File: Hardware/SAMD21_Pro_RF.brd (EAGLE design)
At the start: 40.6 x 30.5 mm, 127 parts, among them J10 AVR_SPI_PROG_3X2TESTPOINTS, J12 JST, J13 U.FL, J7 PTH, J9 External On/Off, U1 MCP73831, U2 915MHz, U4 ATSAMD21G, U5 4MB Flash, U6 3.3V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

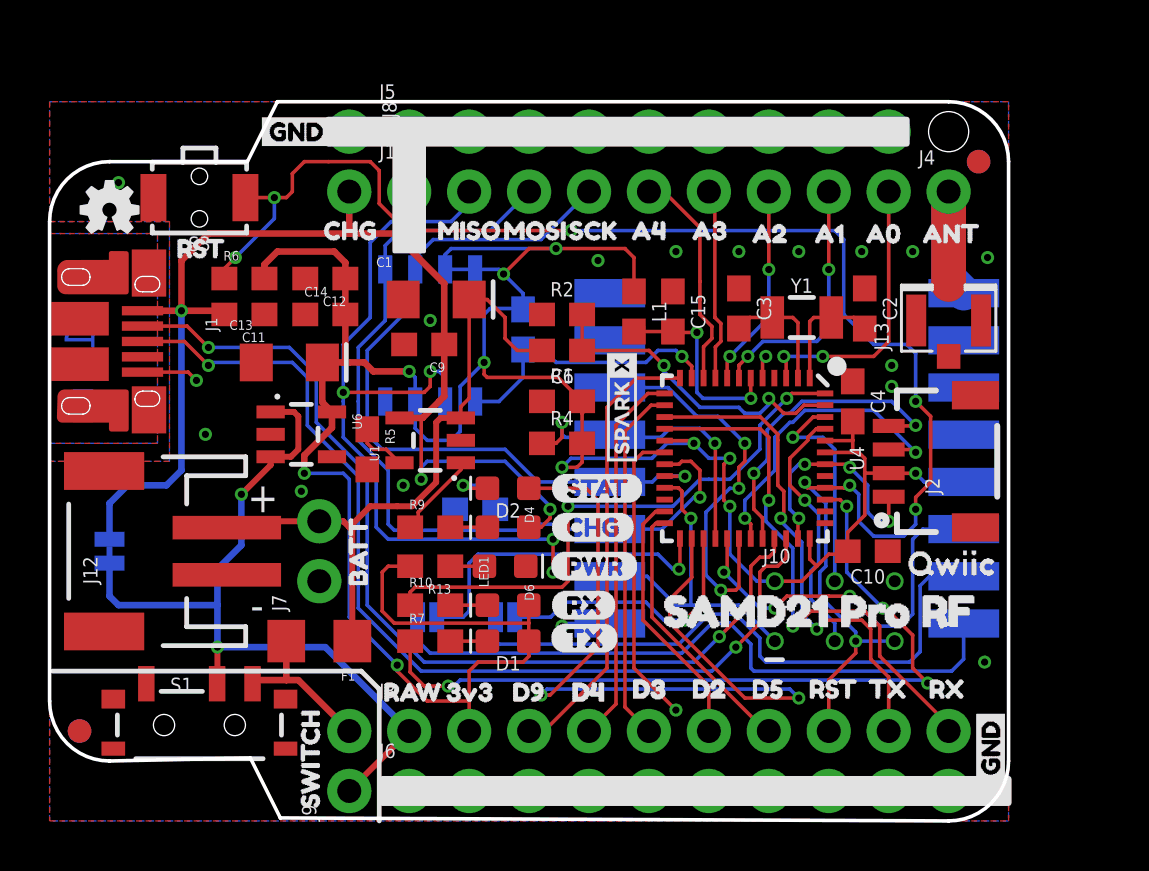
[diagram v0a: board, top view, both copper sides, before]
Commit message: Added Sparkfun labels, correct RFM module (same pinout), fixed silk
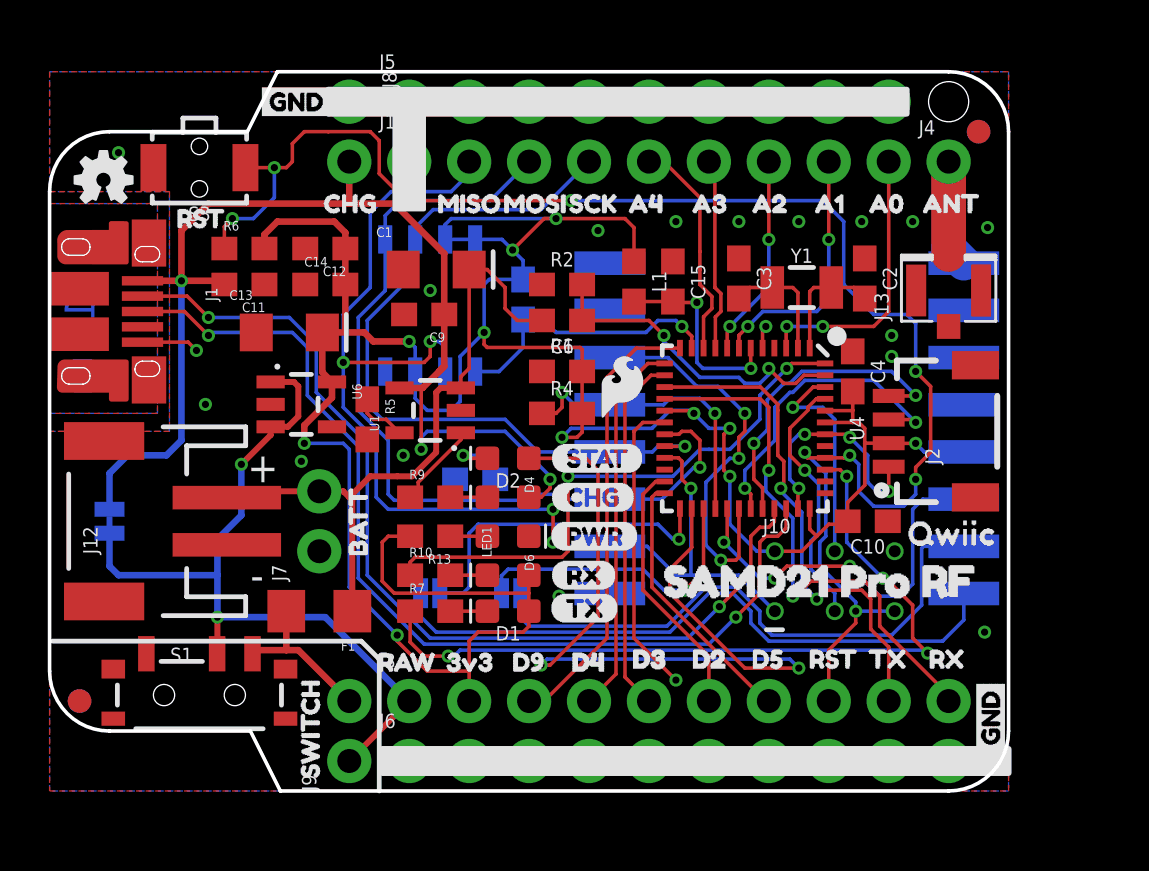
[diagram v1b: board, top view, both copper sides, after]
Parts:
- removed JP1, JP2: (no value), SparkFun-Jumpers:SMT-JUMPER_2_NO_SILK
- removed U$51: (no value), SparkX:SPARKX-MEDIUM
- removed U2: 915MHz, SparkFun-RF:RFM69HCW-XXXS2
- added JP3, JP4: (no value), SparkFun-Jumpers:SMT-JUMPER_2_NO_SILK
- added LOGO2: SFE_LOGO_NAME.1_INCH, SparkFun-Aesthetics:SFE_LOGO_NAME_.1
- added U3: RFM96W, SparkX:RFM95/96/97/98W
- U$34: value SPARKX-LOGO2 -> (none); device SparkX:SPARKX-TINY -> SparkFun-Aesthetics:SFE_LOGO_FLAME_.1
- moved U$30 1.91 mm to (8.38, 16.5)
- moved U$41 1.52 mm to (34.7, 5.59)
- moved U$57 1.52 mm to (37.0, 5.59)
- moved U$19 1.40 mm to (39.5, 5.59)
- moved U$2 1.40 mm to (29.3, 5.59)
- moved U$21 1.40 mm to (26.8, 5.59)
- moved U$33 1.40 mm to (31.8, 5.59)
- moved U$34 1.37 mm to (23.1, 15.5), turned to 0 degrees
- moved U$24 1.30 mm to (13.2, 5.46)
- moved LOGO1 1.30 mm to (2.29, 25.9)
- moved U$61 1.30 mm to (2.29, 25.9)
- moved LED1 1.28 mm to (19.4, 10.8)
- moved U$7 1.28 mm to (34.0, 24.9)
- moved C9 1.27 mm to (15.9, 20.2)
- moved J11 1.27 mm to (15.2, 26.7)
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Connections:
- removed net D10: JP1.2, U4.27
- removed net D11: JP2.2, U4.25
- removed net RFM_IO1: JP1.1, U2.15
- removed net RFM_IO2: JP2.1, U2.16
- new net D10_LORA-WAN: JP3.2, U4.27
- new net D11_LORA-WAN: JP4.2, U4.25
- new net N$17: JP3.1, U3.DIO1
- new net N$18: JP4.1, U3.DIO2
- net !RFM_CS: now also U3.NSS; no longer U2.5
- net 3.3V: now also U3.3.3V; no longer U2.13
- net ANT: now also U3.ANT; no longer U2.9
- net GND: now also U3.GND@1, U3.GND@2, U3.GND@3; no longer U2.1, U2.10, U2.8
- net MISO: now also U3.MISO; no longer U2.2
- net MOSI: now also U3.MOSI; no longer U2.3
- net RFM_INT: now also U3.DIO0; no longer U2.14
- net RFM_RST: now also U3.!RESET; no longer U2.6
- net SCK: now also U3.SCK; no longer U2.4
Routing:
- net RFM_IO2: track 28.0 -> 0.00 mm
- net N$18: track 0.00 -> 27.6 mm
- net RFM_IO1: track 25.9 -> 0.00 mm
- net N$17: track 0.00 -> 24.9 mm
- net D11_LORA-WAN: track 0.00 -> 14.3 mm, vias 0 -> 1
- net D11: track 14.1 -> 0.00 mm, vias 1 -> 0
- net D10_LORA-WAN: track 0.00 -> 12.8 mm, vias 0 -> 1
- net D10: track 11.6 -> 0.00 mm, vias 1 -> 0
- net GND: track 28.2 -> 26.1 mm
- net !RFM_CS: track 13.2 -> 12.7 mm
- net 3.3V: track 121.8 -> 121.2 mm
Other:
- outline, holes or cut-outs redrawn
- board text added: "Units in Inches"

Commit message: More silk fixes
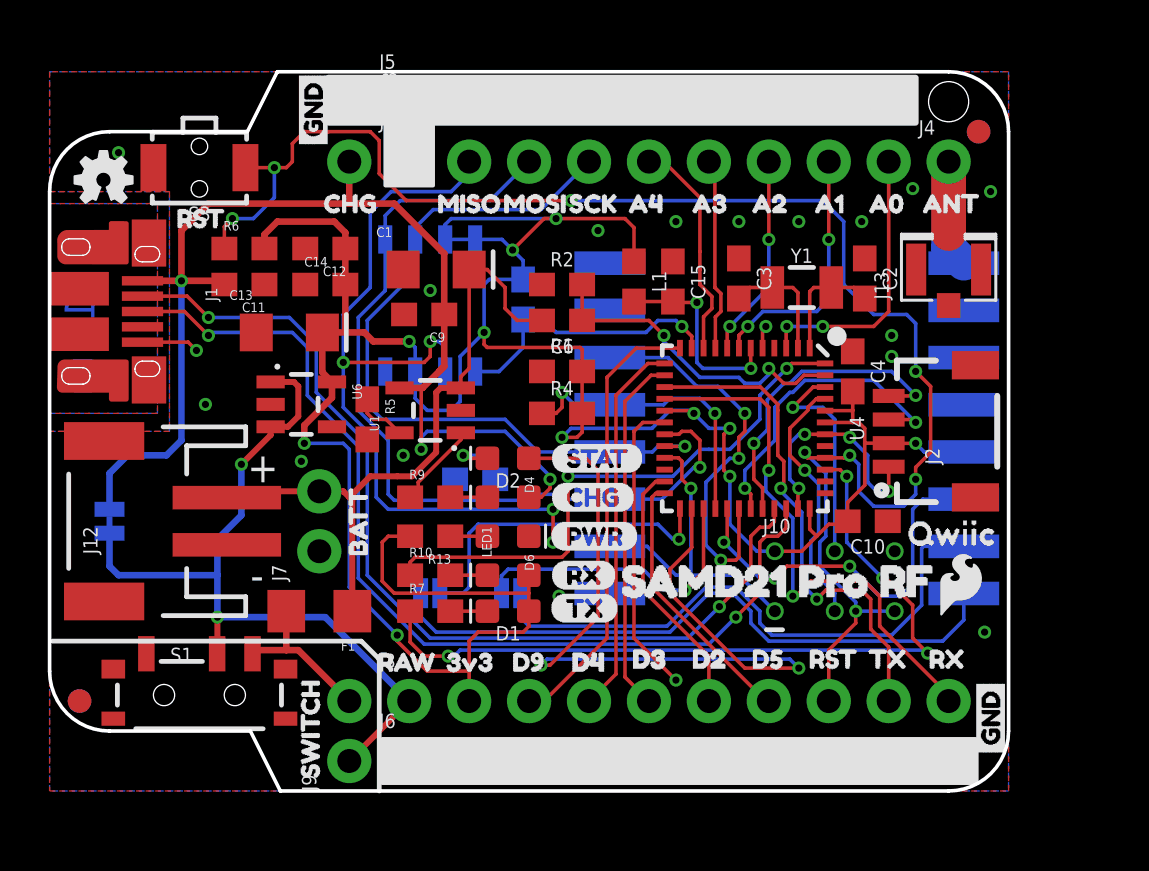
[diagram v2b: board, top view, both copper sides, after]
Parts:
- moved U$34 16.6 mm to (37.5, 7.11)
- moved U$12 3.33 mm to (11.2, 27.1), turned to 90 degrees
- moved U$38 1.81 mm to (11.2, 30.6), turned to 270 degrees
- moved U$1 1.78 mm to (23.1, 8.89)
- moved U$17 1.27 mm to (39.9, 4.95)
- moved J13 0.89 mm to (38.1, 22.1)
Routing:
- net ANT: track 8.50 -> 7.62 mm

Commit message: RX/TX LED Spacing
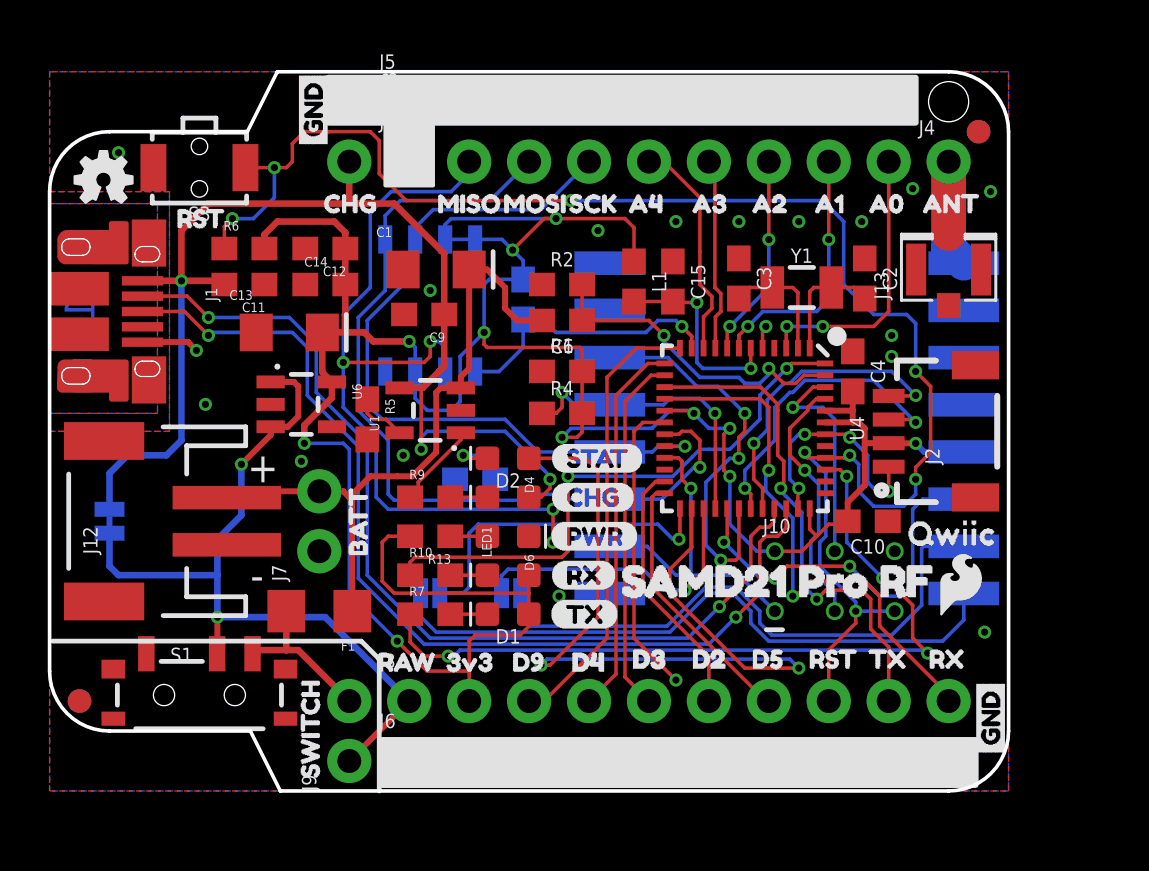
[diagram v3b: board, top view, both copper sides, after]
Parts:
- moved U$70 0.25 mm to (21.2, 7.49)
- moved U$38 0.13 mm to (11.2, 30.7)
- moved D1 0.13 mm to (19.4, 7.49)
- moved R7 0.13 mm to (16.1, 7.49)

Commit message: Removed Flash, added standoffs
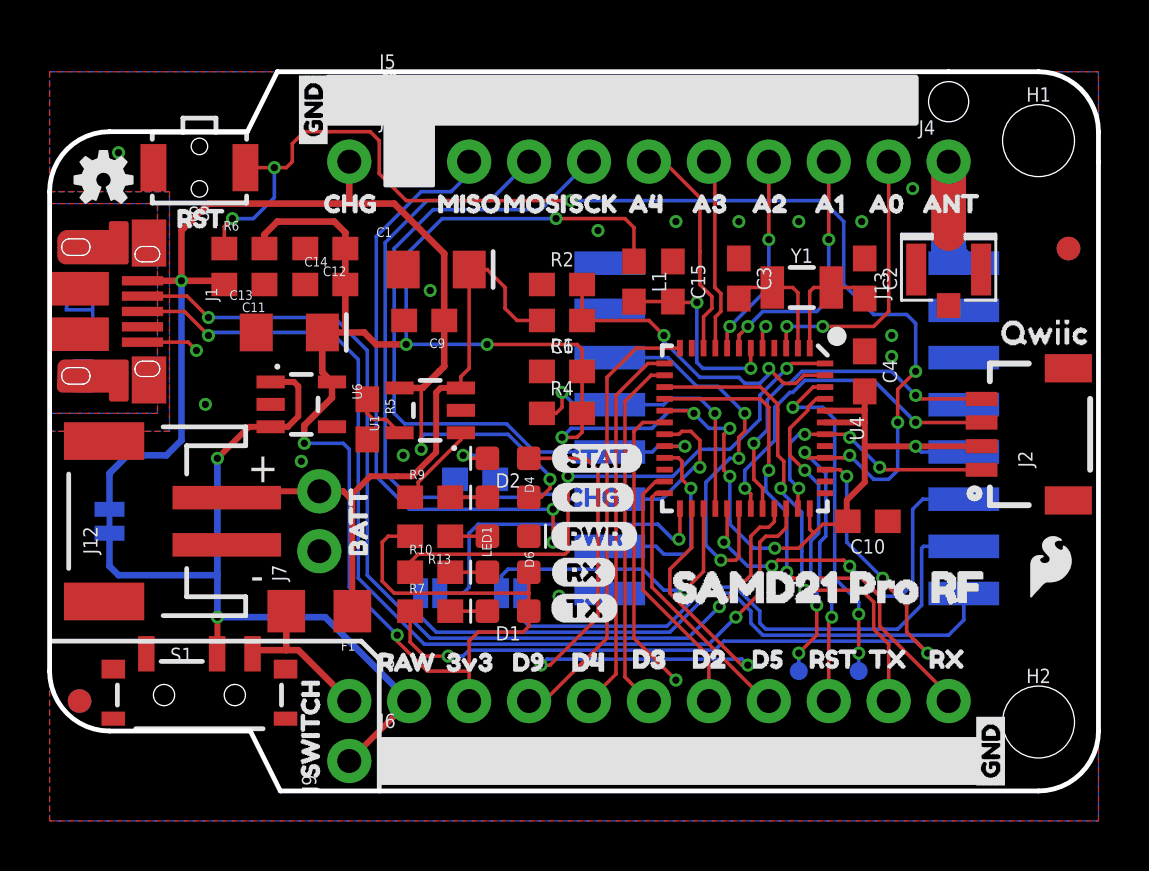
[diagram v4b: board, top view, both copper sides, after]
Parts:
- removed J10: AVR_SPI_PROG_3X2TESTPOINTS, SparkFun-Connectors:2X3_TEST_POINTS
- removed R8: 10k, SparkFun-Resistors:0603
- removed U5: 4MB Flash, SparkFun-IC-Memory:SO08
- added H1, H2: STAND-OFFTIGHT, SparkFun-Hardware:STAND-OFF-TIGHT
- added TP1, TP2: TEST-POINT3, SparkFun-Connectors:PAD.03X.03
- moved U$60 9.38 mm to (39.4, 19.4)
- moved U$30 7.19 mm to (14.2, 20.7)
- moved FD2 6.25 mm to (43.2, 23.0)
- moved FD4 6.25 mm to (43.2, 23.0)
- moved J2 3.94 mm to (39.5, 15.1)
- moved U$34 3.89 mm to (41.3, 7.87)
- moved LOGO2 2.34 mm to (20.2, 13.3)
- moved U$1 2.17 mm to (25.3, 8.64)
- moved U$17 1.40 mm to (39.9, 3.56)
- moved U$62 1.40 mm to (39.9, -0.13)
- moved C4 0.51 mm to (34.5, 17.8)
- moved C9 0.25 mm to (15.9, 19.9)
- moved U$70 0.25 mm to (21.2, 7.75)
- moved U$19 0.13 mm to (39.4, 5.59)
- moved U$38 0.13 mm to (11.2, 30.6)
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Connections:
- net !RST: no longer J10.5
- net 3.3V: no longer J10.2, R8.2, U5.3, U5.7, U5.8
- net D8_!FLASH_CS: no longer R8.1, U5.1
- net GND: no longer J10.6, U5.4
- net MISO: no longer J10.1, U5.2
- net MOSI: no longer U5.5
- net SCK: no longer U5.6
- net SWDCLK: now also TP2.P$1; no longer J10.3
- net SWDIO: now also TP1.P$1; no longer J10.4
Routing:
- net MISO: track 50.2 -> 36.0 mm, vias 5 -> 3
- net D8_!FLASH_CS: track 12.0 -> 0.00 mm, vias 1 -> 0
- net 3.3V: track 121.2 -> 114.6 mm
- net !RST: track 68.3 -> 62.6 mm
- net SWDIO: track 9.30 -> 14.8 mm, vias 1 -> 3
- net STAT_LED: track 34.6 -> 30.1 mm
- net SWDCLK: track 10.9 -> 13.4 mm, vias 1 -> 3
- net MOSI: track 36.8 -> 34.6 mm
- net GND: track 26.1 -> 28.0 mm, vias 23 -> 21
- net SCL: track 13.4 -> 15.1 mm
- net SDA: track 13.3 -> 14.9 mm
- net SCK: track 32.1 -> 30.7 mm
- net D-: track 40.8 -> 41.9 mm
- net RXI: track 23.0 -> 22.0 mm
- net D+: track 41.8 -> 42.8 mm
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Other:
- board size 40.6 x 30.5 mm -> 44.5 x 30.5 mm

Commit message: Post-checklist
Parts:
- removed U$34: (no value), SparkFun-Aesthetics:SFE_LOGO_FLAME_.1
- added U$51: (no value), SparkFun-Aesthetics:SFE_LOGO_FLAME_.2
- U4: device temp:QFN-48_NO_EXPOSED_PAD -> SparkFun-IC-Microcontroller:QFN-48_NO_EXPOSED_PAD
- moved FD2 1.27 mm to (43.2, 24.3)
- moved FD4 1.27 mm to (43.2, 24.3)
- moved TP1 1.27 mm to (34.3, 6.35)
- moved TP2 1.27 mm to (31.8, 6.35)
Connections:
- net RFM_RST renamed !RFM_RST
- removed net D8_!FLASH_CS: U4.11
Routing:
- net STAT_LED: track 30.1 -> 28.3 mm
- net N$18: track 27.4 -> 26.4 mm
- net N$17: track 24.6 -> 23.8 mm
- net 3.3V: track 114.6 -> 114.0 mm

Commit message: Post Review fixes
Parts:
- U3: value RFM96W -> RFM95W; device SparkX:RFM95/96/97/98W -> SparkFun-RF:RFM95/96/97/98W
- moved H1 0.38 mm to (41.9, 27.9)
- moved H2 0.38 mm to (41.9, 2.54)
- moved U$24 0.28 mm to (13.5, 5.59)
- moved U$17 0.25 mm to (39.9, 3.30)
- moved U$62 0.25 mm to (39.9, -0.38)
- moved U$11 0.13 mm to (36.2, 24.9)
- moved U$73 0.13 mm to (36.7, 5.59)
- moved U$9 0.13 mm to (18.4, 24.9)
- moved U$15 0.13 mm to (18.9, 5.59)
- moved U$16 0.13 mm to (21.6, 5.59)
- moved U$22 0.13 mm to (21.5, 5.59)
- moved U$23 0.13 mm to (16.1, 5.59)
- moved U$31 0.13 mm to (24.3, 5.59)
- moved U$52 0.13 mm to (17.0, 5.59)
- moved U$53 0.13 mm to (19.4, 5.59)
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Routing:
- net SHLD: track 0.00 -> 2.39 mm, vias 0 -> 2

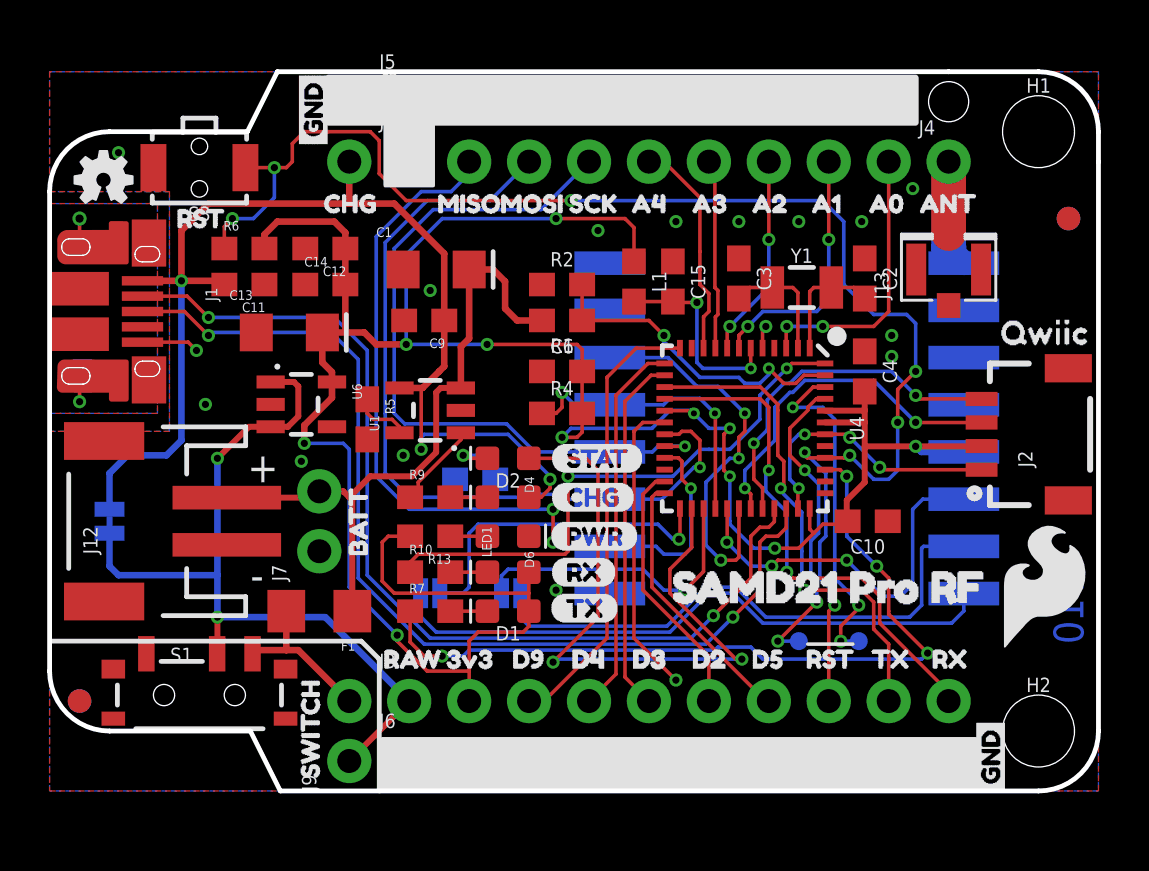
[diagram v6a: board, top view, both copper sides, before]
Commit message: Issues caught
Replaced 10k resistors with 1M Ohm resistors, added Mosfet circuit, moved decoupling capacitors in schematic to more clearly reflect their placement on the board, and removed jumper from RAW line. All power lines have been updated with better labels.
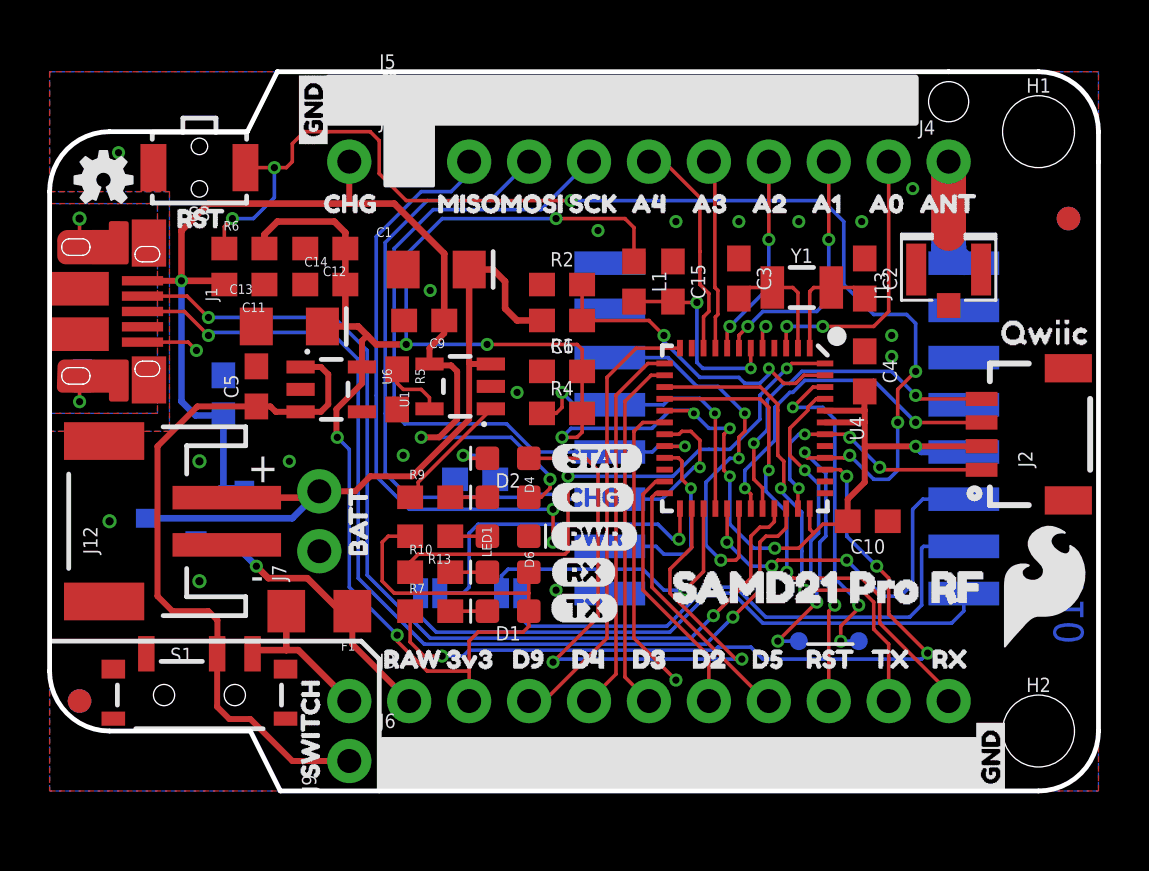
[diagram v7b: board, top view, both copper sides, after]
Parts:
- removed SJ2: USB Power, SparkFun-Jumpers:SMT-JUMPER_2_NC_TRACE_SILK
- removed U$58: (no value), CUTIFRAW:CUT_IF_RAW_IN0
- removed U$59: (no value), GREATER:GREATER_THAN_5#5V0
- added C5: 1.0uF, SparkFun-Capacitors:0603
- added D3: BAT20J, SparkFun-DiscreteSemi:SOD-323
- added Q1: 2.5A/30V, SparkFun-DiscreteSemi:SOT23-3
- added R8: 10k, SparkFun-Resistors:0603
- R1, R2: value 10k -> 1M
- moved R5 1.80 mm to (14.7, 17.0)
- moved U1 1.63 mm to (17.4, 17.1)
- moved U6 1.42 mm to (11.9, 17.0)
- moved U$37 1.14 mm to (11.0, 5.33)
- moved C13 0.25 mm to (10.2, 19.7)
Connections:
- removed net USB_VCC: C11.2, C9.1, D4.A, J1.VBUS, J8.2, SJ2.2, U1.4
- removed net VBATT: C1.+, F1.1, J12.2, J7.2, R1.2, U1.3
- new net VIN: C5.1, J9.1, S1.2, U6.1, U6.3
- new net V_BATT: C1.+, J12.2, J7.2, Q1.3, R1.2, U1.3
- new net V_USB: C11.2, C9.1, D3.A, D4.A, J1.VBUS, J8.2, Q1.1, R8.2, U1.4
- net GND: now also C5.2, R8.1
- net RAW: now also D3.C, F1.1, Q1.2; no longer J9.1, S1.2, SJ2.1, U6.1, U6.3
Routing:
- net V_USB: track 0.00 -> 50.2 mm, vias 0 -> 3
- net USB_VCC: track 49.8 -> 0.00 mm, vias 3 -> 0
- net V_BATT: track 0.00 -> 31.4 mm
- net VIN: track 0.00 -> 30.3 mm
- net VBATT: track 28.2 -> 0.00 mm
- net RAW: track 34.3 -> 13.0 mm, vias 2 -> 1
- net 3.3V: track 114.0 -> 111.8 mm
- net CHARGE_STAT: track 3.62 -> 5.17 mm
- net GND: vias 21 -> 24
